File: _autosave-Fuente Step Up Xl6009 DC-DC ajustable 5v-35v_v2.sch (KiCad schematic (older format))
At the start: 16 parts, among them J1 Screw_Terminal_01x02, J2 Screw_Terminal_01x02, U1 XL6009E1

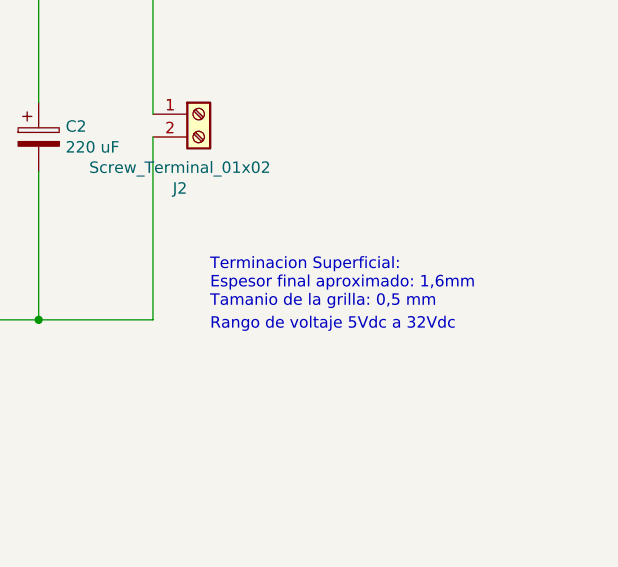
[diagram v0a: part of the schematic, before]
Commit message: Se modificaron las posiciones de los componentes de acuerdo a la recomencadion del companiero y se rutearon nuevamente algunas pistas
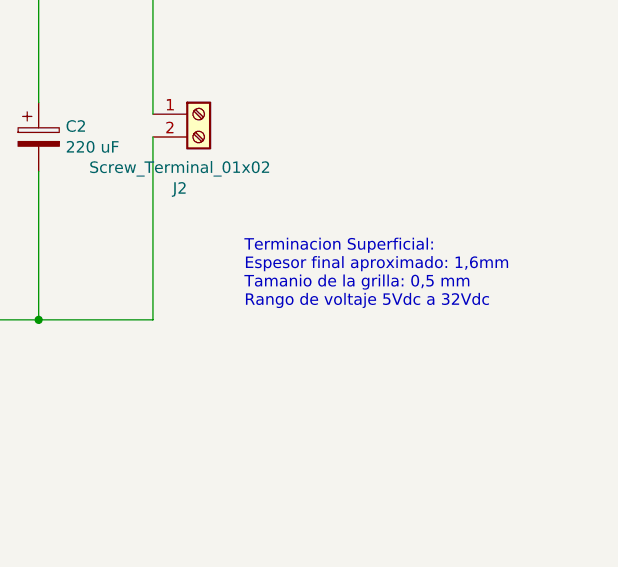
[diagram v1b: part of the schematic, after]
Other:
- note added: "Terminacion Superficial:\nEspesor final aproximado: 1,6mm\nTamanio de la grilla: 0,5 mm\nRango de voltaje 5Vdc a 32Vdc"
- note removed: "Rango de voltaje 5Vdc a 32Vdc"
- note removed: "Terminacion Superficial:\nEspesor final aproximado: 1,6mm\nTamanio de la grilla: 0,5 mm"
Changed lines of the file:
@@
 	7600 3900 7100 3900
 Connection ~ 7100 3900
-Text Notes 7850 3850 0    50   ~ 0
-Terminacion Superficial:\nEspesor final aproximado: 1,6mm\nTamanio de la grilla: 0,5 mm
-Text Notes 7850 3950 0    50   ~ 0
-Rango de voltaje 5Vdc a 32Vdc
 $Comp
 L Mechanical:MountingHole H1
@@
 	1    0    0    -1
 $EndComp
+Text Notes 8000 3850 0    50   ~ 0
+Terminacion Superficial:\nEspesor final aproximado: 1,6mm\nTamanio de la grilla: 0,5 mm\nRango de voltaje 5Vdc a 32Vdc
 $EndSCHEMATC
